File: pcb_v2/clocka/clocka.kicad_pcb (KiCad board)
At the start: 2 copper layers, 114.3 x 125 mm, 63 parts, among them J2 control panel, J26 bus clock, J3 control panel, U1 74LS74, U10 74LS125, U11 NE555P, U12 NE555P, U2 74LS74, U3 74LS74, U4 74LS04, U5 74LS125, U6 74LS86, U7 74LS08, U8 NE555P, U9 NE555P, Y1 XTAL1, Y2 XTAL2

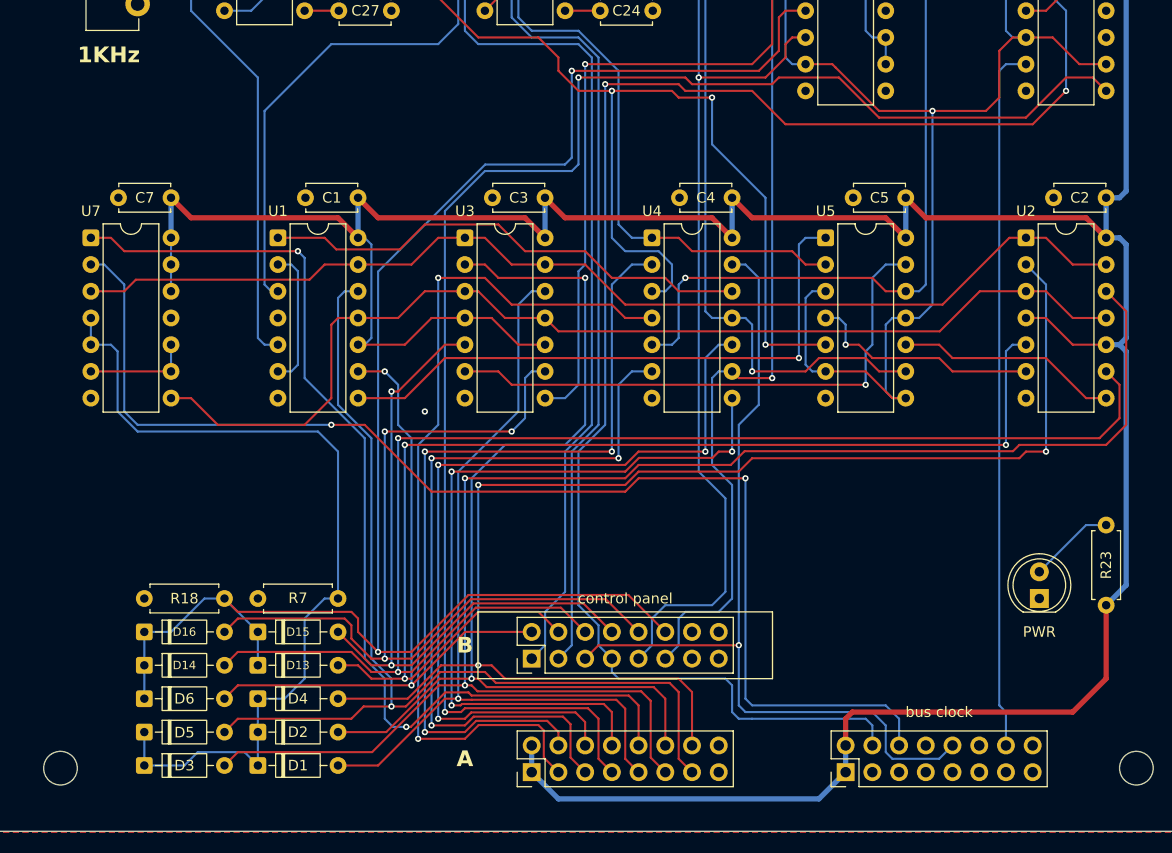
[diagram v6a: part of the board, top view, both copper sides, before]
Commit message: conector reposicionado para ser compatível com a sysbus
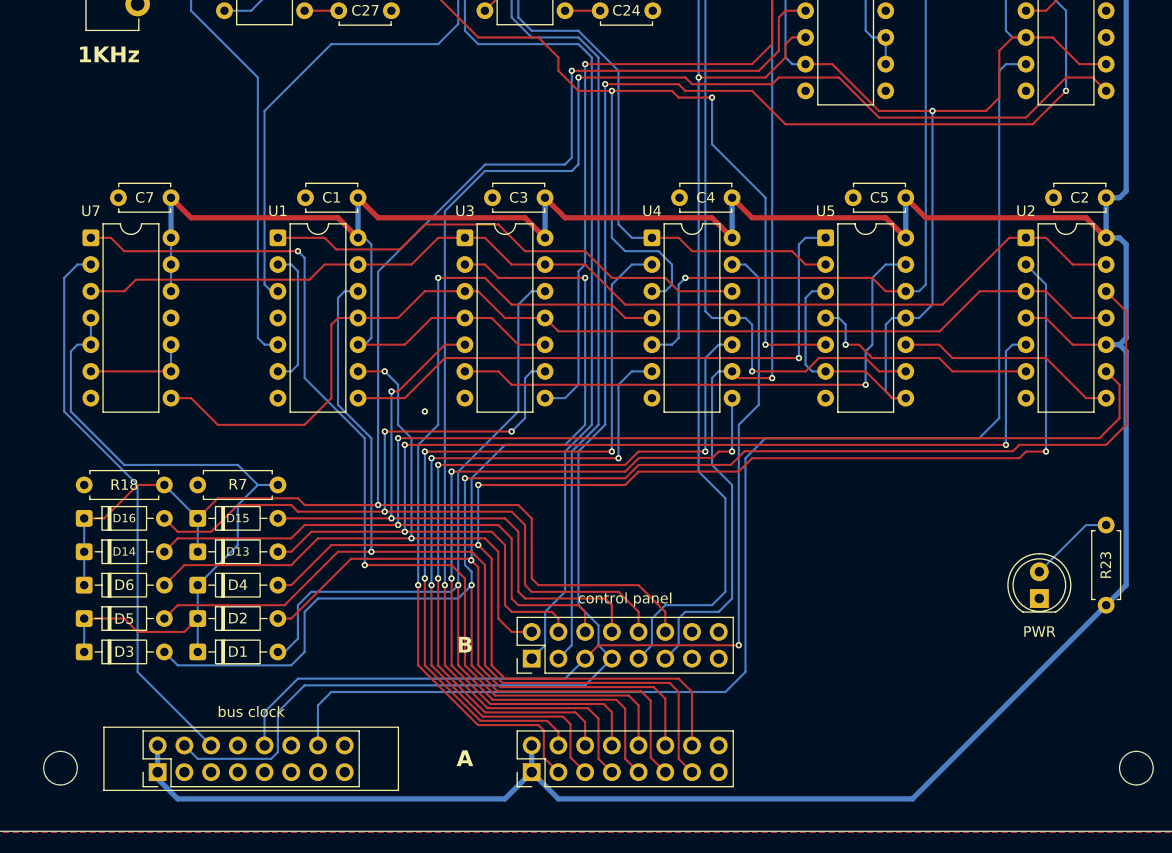
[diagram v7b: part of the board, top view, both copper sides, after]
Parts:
- moved J26 65.4 mm to (184.2, 148.0)
- moved D2 12.2 mm to (188.0, 133.3)
- moved D5 12.2 mm to (177.2, 133.3)
- moved D15 12.2 mm to (188.0, 123.8)
- moved D16 12.2 mm to (177.2, 123.8)
- moved D1 12.2 mm to (188.0, 136.5)
- moved D13 12.2 mm to (188.0, 127.0)
- moved D14 12.2 mm to (177.2, 127.0)
- moved D3 12.2 mm to (177.2, 136.5)
- moved D4 12.2 mm to (188.0, 130.2)
- moved D6 12.2 mm to (177.2, 130.2)
- moved R18 12.2 mm to (184.8, 120.7)
- moved R7 12.2 mm to (195.6, 120.7)
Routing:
- net ~{control_break}: track 117.7 -> 53.3 mm, vias 2 -> 0
- net ~{CLOCK}: track 67.2 -> 127.6 mm
- net +5V: track 604.9 -> 638.4 mm
- net Net-(D1-K): track 83.8 -> 66.3 mm
- net CLOCK: track 147.7 -> 163.5 mm
- net set_clock_xtal1: track 149.8 -> 157.4 mm
- net ~{clock_manual}: track 165.2 -> 157.7 mm
- net set_clock_ext: track 79.8 -> 85.5 mm
- net RESET: track 84.1 -> 89.7 mm
- net ~{operator_break}: track 98.2 -> 92.9 mm
- net set_clock_1Khz: track 132.1 -> 137.3 mm
- net Net-(J2-Pin_3): track 83.7 -> 78.6 mm
- net set_clock_xtal2: track 96.3 -> 101.2 mm
- net Net-(J2-Pin_4): track 79.8 -> 75.2 mm
- net Net-(J2-Pin_5): track 72.9 -> 68.8 mm
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
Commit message: continuando implementação do clock
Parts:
- removed D15, D2: 1N4148, Diode_THT:D_DO-35_SOD27_P7.62mm_Horizontal
- removed Y2: XTAL2, Oscillator:Oscillator_DIP-8
- added R1: 1K, Resistor_THT:R_Axial_DIN0207_L6.3mm_D2.5mm_P7.62mm_Horizontal, F.Cu at (210.6, 148.6)
- added R2: 1K, Resistor_THT:R_Axial_DIN0207_L6.3mm_D2.5mm_P7.62mm_Horizontal, F.Cu at (214.6, 148.6)
- moved D3 70.9 mm to (247.0, 148.6), turned to 90 degrees
- moved D5 68.4 mm to (243.8, 148.6), turned to 90 degrees
- moved D6 66.1 mm to (240.7, 148.6), turned to 90 degrees
- moved D14 64.1 mm to (237.5, 148.6), turned to 90 degrees
- moved D16 62.3 mm to (234.3, 148.6), turned to 90 degrees
- moved D1 44.8 mm to (231.1, 148.6), turned to 90 degrees
- moved D4 44.0 mm to (228.0, 148.6), turned to 90 degrees
- moved D13 42.7 mm to (224.8, 148.6), turned to 90 degrees
- moved R18 42.1 mm to (221.6, 141.0), turned to -90 degrees
- moved J2 38.7 mm to (257.8, 141.0)
- moved J3 38.7 mm to (257.8, 130.2)
- moved R7 30.6 mm to (218.4, 141.0), turned to -90 degrees
- moved D7 30.5 mm to (298.4, 132.1)
- moved R23 29.2 mm to (303.5, 132.7)
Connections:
- J2 pad 12: set_clock_xtal2 -> unconnected-(J2-Pin_12-Pad12)
- J2 pad 5: Net-(J2-Pin_5) -> unconnected-(J2-Pin_5-Pad5)
- J3 pad 8: clock_xtal2 -> unconnected-(J3-Pin_8-Pad8)
- U3 pad 1: ~{disengage_clock} -> +5V
- U3 pad 2: set_clock_xtal2 -> +5V
- U3 pad 3: set_clock_source -> +5V
- U3 pad 5: clock_xtal2 -> unconnected-(U3A-Q-Pad5)
- U3 pad 6: ~{clock_xtal2} -> unconnected-(U3A-~{Q}-Pad6)
- U4 pad 5: signal_xtal2 -> +5V
- U4 pad 6: Net-(J2-Pin_5) -> unconnected-(U4-Pad6)
- U5 pad 11: combined_clock -> unconnected-(U5-Pad11)
- U5 pad 12: signal_xtal2 -> +5V
- U5 pad 13: ~{clock_xtal2} -> +5V
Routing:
- net (no net): track 0.00 -> 182.5 mm, vias 0 -> 5
- net set_clock_xtal2: track 101.2 -> 0.00 mm, vias 2 -> 0
- net signal_xtal2: track 99.4 -> 0.00 mm, vias 1 -> 0
- net Net-(J2-Pin_5): track 68.8 -> 0.00 mm, vias 3 -> 0
- net +5V: track 638.4 -> 707.1 mm, vias 0 -> 4
- net RESET: track 89.7 -> 25.5 mm, vias 1 -> 0
- net clock_xtal2: track 61.9 -> 0.00 mm, vias 2 -> 0
- net ~{CLOCK}: track 127.6 -> 67.1 mm
- net ~{clock_xtal2}: track 52.8 -> 0.00 mm, vias 1 -> 0
- net Net-(D1-K): track 66.3 -> 28.4 mm
- net Net-(J2-Pin_4): track 75.2 -> 106.2 mm
- net Net-(J2-Pin_3): track 78.6 -> 109.5 mm
- net Net-(J2-Pin_6): track 75.4 -> 106.3 mm
- net ~{operator_break}: track 92.9 -> 123.6 mm
- net ~{operator_break_enable}: track 142.7 -> 173.4 mm
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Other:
- outline, holes or cut-outs redrawn
